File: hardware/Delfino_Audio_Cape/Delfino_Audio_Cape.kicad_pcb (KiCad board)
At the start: 2 copper layers, 143.8 x 162.6 mm, 125 parts, among them J1 JACK_PJ324, J1-J1 Conn_02x10_Odd_Even, J1-J2 Conn_02x10_Odd_Even, J1-J3 Conn_02x10_Odd_Even, J1-J4 Conn_02x10_Odd_Even, J2 JACK_PJ324, J3 JACK_PJ324, J4 PWR, J5 JACK_PJ324, J8 JACK_PJ324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

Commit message: Cambios en el PCB
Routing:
- net +12V: track 729.6 -> 728.8 mm, vias 10 -> 9
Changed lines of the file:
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@@
   (general
     (links 216)
-    (no_connects 0)
+    (no_connects 71)
     (area 111.589943 42.766 277.903715 223.595001)
     (thickness 1.6)
@@
   (segment (start 143.4338 145.2226) (end 143.4338 149.352) (width 0.889) (layer B.Cu) (net 3) (status 20))
   (segment (start 143.4338 149.352) (end 143.3576 149.4282) (width 0.889) (layer B.Cu) (net 3) (status 30))
+  (segment (start 179.8574 138.7348) (end 179.8574 126.9746) (width 2.032) (layer B.Cu) (net 4))
+  (segment (start 179.8574 126.9746) (end 180.213 126.619) (width 2.032) (layer B.Cu) (net 4))
+  (via (at 180.213 126.619) (size 2.54) (drill 0.4) (layers F.Cu B.Cu) (net 4))
+  (segment (start 178.689 82.169) (end 191.389 82.169) (width 2.032) (layer B.Cu) (net 4))
+  (segment (start 197.612 75.946) (end 197.612 64.008) (width 2.032) (layer B.Cu) (net 4))
+  (segment (start 191.389 82.169) (end 197.612 75.946) (width 2.032) (layer B.Cu) (net 4))
+  (segment (start 149.8346 203.0222) (end 119.7356 203.0222) (width 1.27) (layer F.Cu) (net 4))
   (segment (start 171.323 77.851) (end 145.4658 77.851) (width 2.032) (layer B.Cu) (net 4))
   (segment (start 145.4658 77.851) (end 144.8181 78.4987) (width 2.032) (layer B.Cu) (net 4))
@@
   (segment (start 231.394 126.238) (end 180.594 126.238) (width 1.27) (layer F.Cu) (net 4))
   (segment (start 233.1466 124.4854) (end 231.394 126.238) (width 1.27) (layer F.Cu) (net 4))
-  (via (at 178.816 82.296) (size 2.54) (drill 0.4) (layers F.Cu B.Cu) (net 4))
-  (segment (start 197.612 64.008) (end 197.612 77.47) (width 2.032) (layer F.Cu) (net 4))
-  (segment (start 193.04 82.042) (end 197.612 77.47) (width 2.032) (layer F.Cu) (net 4))
-  (segment (start 179.07 82.042) (end 193.04 82.042) (width 2.032) (layer F.Cu) (net 4))
-  (segment (start 179.07 82.042) (end 178.816 82.296) (width 2.032) (layer F.Cu) (net 4))
   (segment (start 233.5276 209.8802) (end 233.5276 207.1116) (width 1.27) (layer F.Cu) (net 4))
   (segment (start 213.36 205.74) (end 179.8574 172.2374) (width 2.032) (layer F.Cu) (net 4))
@@
   (segment (start 180.086 122.555) (end 187.833 114.808) (width 2.032) (layer F.Cu) (net 4))
   (segment (start 180.086 126.619) (end 180.213 126.619) (width 1.27) (layer F.Cu) (net 4))
-  (segment (start 179.8574 138.7348) (end 179.8574 126.9746) (width 2.032) (layer B.Cu) (net 4))
   (segment (start 199.136 147.32) (end 199.136 147.066) (width 1.27) (layer F.Cu) (net 4))
   (segment (start 199.136 147.066) (end 179.324 127.254) (width 2.032) (layer F.Cu) (net 4))
@@
   (segment (start 180.34 126.492) (end 180.34 126.238) (width 2.032) (layer F.Cu) (net 4))
   (segment (start 180.213 126.619) (end 180.34 126.492) (width 2.032) (layer F.Cu) (net 4))
-  (via (at 180.213 126.619) (size 2.54) (drill 0.4) (layers F.Cu B.Cu) (net 4))
-  (segment (start 179.8574 126.9746) (end 180.213 126.619) (width 2.032) (layer B.Cu) (net 4))
   (via (at 188.722 94.742) (size 2.54) (drill 0.4) (layers F.Cu B.Cu) (net 4))
   (segment (start 188.722 94.742) (end 184.404 99.06) (width 2.032) (layer B.Cu) (net 4))
@@
   (segment (start 220.9546 88.0872) (end 220.9546 90.7034) (width 1.27) (layer F.Cu) (net 4))
   (segment (start 171.323 77.851) (end 174.371 77.851) (width 2.032) (layer B.Cu) (net 4))
-  (segment (start 174.371 77.851) (end 178.816 82.296) (width 2.032) (layer B.Cu) (net 4))
+  (segment (start 174.371 77.851) (end 178.689 82.169) (width 2.032) (layer B.Cu) (net 4))
+  (segment (start 178.689 82.169) (end 178.816 82.296) (width 2.032) (layer B.Cu) (net 4))
   (segment (start 178.816 82.296) (end 178.308 81.788) (width 2.032) (layer B.Cu) (net 4))
   (segment (start 178.308 81.788) (end 178.308 99.06) (width 2.032) (layer B.Cu) (net 4))
@@
   (segment (start 119.7356 203.0222) (end 123.2916 199.4662) (width 1.27) (layer B.Cu) (net 4))
   (via (at 119.7356 203.0222) (size 2.54) (drill 0.4) (layers F.Cu B.Cu) (net 4))
-  (segment (start 149.8346 203.0222) (end 119.7356 203.0222) (width 1.27) (layer F.Cu) (net 4))
   (via (at 149.8346 203.0222) (size 2.54) (drill 0.4) (layers F.Cu B.Cu) (net 4))
   (segment (start 149.8346 202.8952) (end 149.8346 203.0222) (width 1.27) (layer B.Cu) (net 4))
@@
   (segment (start 122.1496 178.1662) (end 121.6496 178.6662) (width 0.889) (layer B.Cu) (net 13))
   (segment (start 220.298 154.94) (end 201.1426 154.94) (width 1.27) (layer F.Cu) (net 14))
-  (segment (start 163.5486 117.346) (end 158.464 117.346) (width 1.27) (layer F.Cu) (net 14))
   (segment (start 201.1426 154.94) (end 163.5486 117.346) (width 1.27) (layer F.Cu) (net 14))
+  (segment (start 163.5486 117.346) (end 158.464 117.346) (width 1.27) (layer F.Cu) (net 14))
   (segment (start 141.3256 175.4162) (end 141.2456 175.4162) (width 0.889) (layer B.Cu) (net 15))
   (segment (start 141.2456 175.4162) (end 137.7696 178.8922) (width 0.889) (layer B.Cu) (net 15))
@@
   (segment (start 144.1196 180.4162) (end 141.3256 180.4162) (width 0.889) (layer B.Cu) (net 16))
   (segment (start 144.1196 193.8782) (end 144.1196 198.4502) (width 0.889) (layer B.Cu) (net 17))
+  (segment (start 132.0546 205.3082) (end 132.0546 203.2254) (width 0.889) (layer B.Cu) (net 18))
+  (segment (start 137.7696 197.5104) (end 137.7696 191.3382) (width 0.889) (layer B.Cu) (net 18))
+  (segment (start 132.0546 203.2254) (end 137.7696 197.5104) (width 0.889) (layer B.Cu) (net 18))
   (segment (start 132.0546 210.7692) (end 132.0546 205.3082) (width 0.889) (layer B.Cu) (net 18))
-  (segment (start 137.7696 191.3382) (end 137.7696 199.5932) (width 0.889) (layer B.Cu) (net 18))
-  (segment (start 137.7696 199.5932) (end 132.0546 205.3082) (width 0.889) (layer B.Cu) (net 18))
   (segment (start 128.27 162.052) (end 128.27 154.9038) (width 1.27) (layer B.Cu) (net 19))
   (segment (start 128.27 154.9038) (end 128.4116 154.7622) (width 1.27) (layer B.Cu) (net 19))
@@
     (connect_pads (clearance 0.508))
     (min_thickness 0.254)
-    (fill yes (arc_segments 16) (thermal_gap 0.508) (thermal_bridge_width 0.508))
+    (fill (arc_segments 16) (thermal_gap 0.508) (thermal_bridge_width 0.508))
     (polygon
       (pts
@@
     (connect_pads (clearance 0.508))
     (min_thickness 0.254)
-    (fill yes (arc_segments 16) (thermal_gap 0.508) (thermal_bridge_width 0.508))
+    (fill (arc_segments 16) (thermal_gap 0.508) (thermal_bridge_width 0.508))
     (polygon
       (pts
@@
     (connect_pads (clearance 0.508))
     (min_thickness 0.254)
-    (fill yes (arc_segments 16) (thermal_gap 0.508) (thermal_bridge_width 0.508))
+    (fill (arc_segments 16) (thermal_gap 0.508) (thermal_bridge_width 0.508))
     (polygon
       (pts
@@
     (connect_pads (clearance 0.508))
     (min_thickness 0.254)
-    (fill yes (arc_segments 16) (thermal_gap 0.508) (thermal_bridge_width 0.508))
+    (fill (arc_segments 16) (thermal_gap 0.508) (thermal_bridge_width 0.508))
     (polygon
       (pts
@@
     (connect_pads (clearance 0.508))
     (min_thickness 0.254)
-    (fill yes (arc_segments 16) (thermal_gap 0.508) (thermal_bridge_width 0.508))
+    (fill (arc_segments 16) (thermal_gap 0.508) (thermal_bridge_width 0.508))
     (polygon
       (pts
@@
     (connect_pads (clearance 0.508))
     (min_thickness 0.254)
-    (fill yes (arc_segments 16) (thermal_gap 0.508) (thermal_bridge_width 0.508))
+    (fill (arc_segments 16) (thermal_gap 0.508) (thermal_bridge_width 0.508))
     (polygon
       (pts
@@
     (connect_pads (clearance 0.508))
     (min_thickness 0.254)
-    (fill yes (arc_segments 16) (thermal_gap 0.508) (thermal_bridge_width 0.508))
+    (fill (arc_segments 16) (thermal_gap 0.508) (thermal_bridge_width 0.508))
     (polygon
       (pts
@@
     (connect_pads (clearance 0.508))
     (min_thickness 0.254)
-    (fill yes (arc_segments 16) (thermal_gap 0.508) (thermal_bridge_width 0.508))
+    (fill (arc_segments 16) (thermal_gap 0.508) (thermal_bridge_width 0.508))
     (polygon
       (pts
@@
     (connect_pads (clearance 0.508))
     (min_thickness 0.254)
-    (fill yes (arc_segments 16) (thermal_gap 0.508) (thermal_bridge_width 0.508))
+    (fill (arc_segments 16) (thermal_gap 0.508) (thermal_bridge_width 0.508))
     (polygon
       (pts
@@
     (connect_pads (clearance 0.508))
     (min_thickness 0.254)
-    (fill yes (arc_segments 16) (thermal_gap 0.508) (thermal_bridge_width 0.508))
+    (fill (arc_segments 16) (thermal_gap 0.508) (thermal_bridge_width 0.508))
     (polygon
       (pts
@@
     (connect_pads (clearance 0.508))
     (min_thickness 0.254)
-    (fill yes (arc_segments 16) (thermal_gap 0.508) (thermal_bridge_width 0.508))
+    (fill (arc_segments 16) (thermal_gap 0.508) (thermal_bridge_width 0.508))
     (polygon
       (pts
@@
     (connect_pads (clearance 0.508))
     (min_thickness 0.254)
-    (fill yes (arc_segments 16) (thermal_gap 0.508) (thermal_bridge_width 0.508))
+    (fill (arc_segments 16) (thermal_gap 0.508) (thermal_bridge_width 0.508))
     (polygon
       (pts
@@
     (connect_pads (clearance 0.508))
     (min_thickness 0.254)
-    (fill yes (arc_segments 16) (thermal_gap 0.508) (thermal_bridge_width 0.508))
+    (fill (arc_segments 16) (thermal_gap 0.508) (thermal_bridge_width 0.508))
     (polygon
       (pts
@@
     (connect_pads (clearance 0.508))
     (min_thickness 0.254)
-    (fill yes (arc_segments 16) (thermal_gap 0.508) (thermal_bridge_width 0.508))
+    (fill (arc_segments 16) (thermal_gap 0.508) (thermal_bridge_width 0.508))
     (polygon
       (pts

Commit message: Cambios en el PCB
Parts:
- moved R17 13.7 mm to (153.4, 150.2), turned to 180 degrees
- moved C12 0.20 mm to (148.3, 136.1), turned to 0 degrees
- moved R30 0.20 mm to (123.2, 195.1)
- moved R31 0.20 mm to (127.8, 195.1)
- moved C18 0.20 mm to (149.4, 191.5), turned to 0 degrees
- moved R27 0.13 mm to (144.0, 215.4)
- moved TP15 0.08 mm to (254.1, 190.5)
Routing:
- net +12V: track 728.8 -> 647.3 mm, vias 9 -> 10
- net /ADC_A2: track 65.3 -> 79.1 mm
- net /ADC_A0: track 83.0 -> 76.8 mm, vias 0 -> 2
- net +3V3: track 82.6 -> 88.1 mm, vias 2 -> 4
- net GND: track 5.67 -> 10.4 mm
- net /ADC_B1: track 105.1 -> 107.4 mm, vias 1 -> 2
- added copper zone on B.Cu, net GND
- removed copper zone on F.Cu, net GND
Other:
- net class D1 added: clearance 0.2032, trace_width 0.889, via_dia 2.54, via_drill 0.4
- net class Default: clearance 0.4572 -> 0.508
- rule trace_clearance: 0.4572 -> 0.508

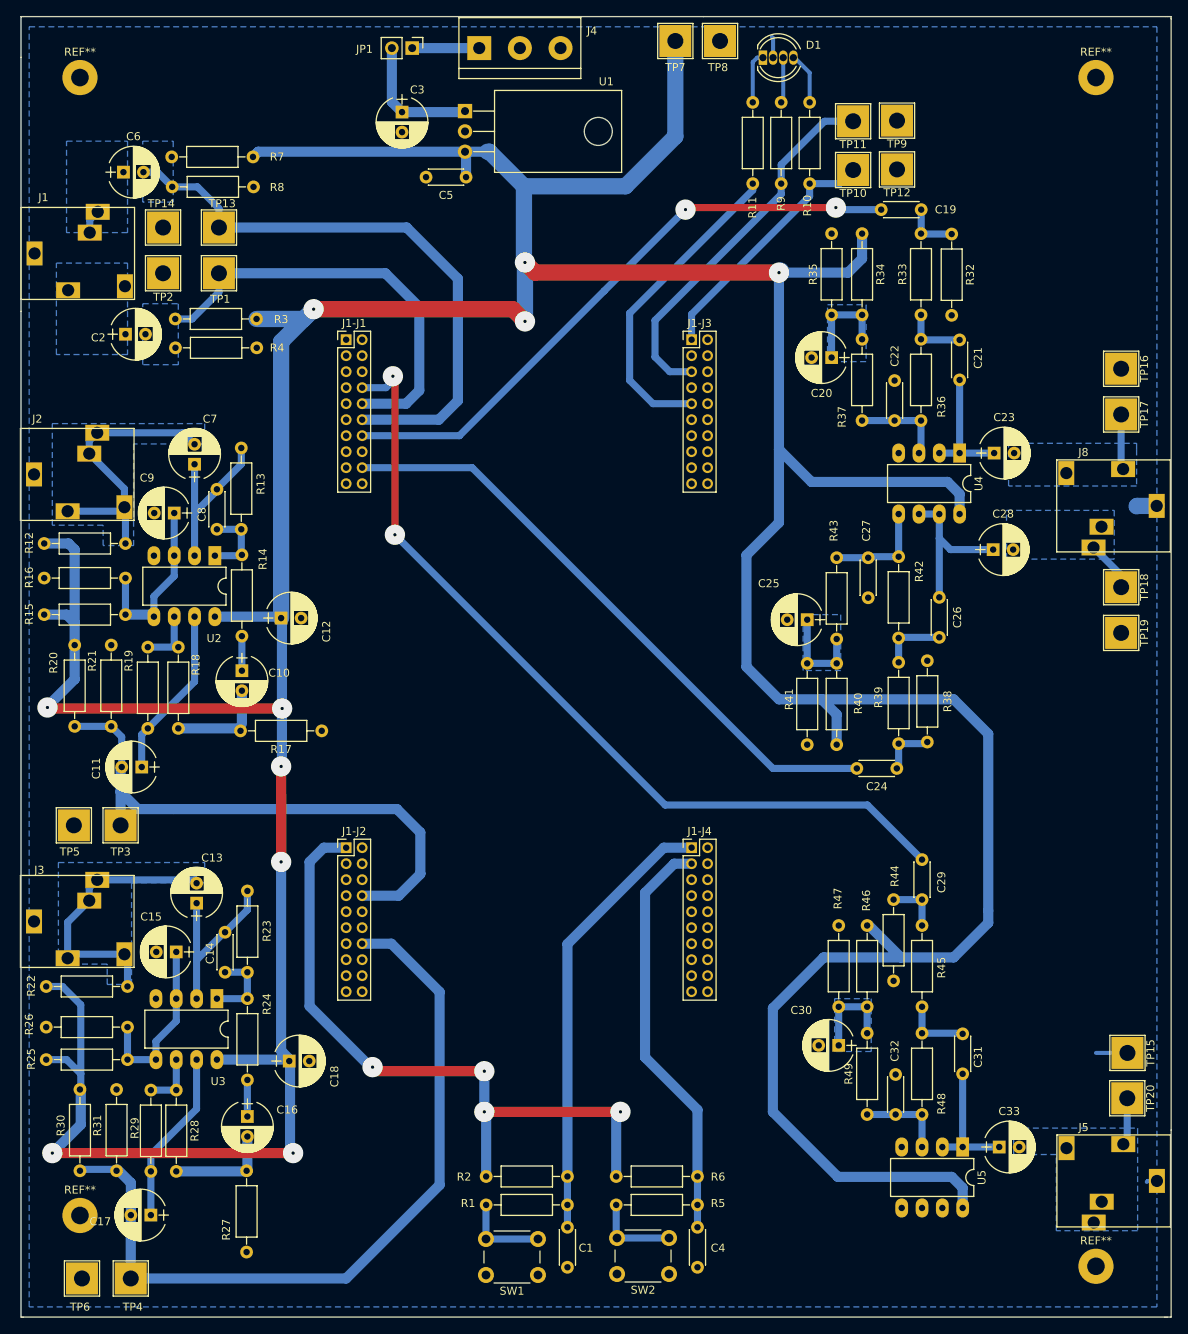
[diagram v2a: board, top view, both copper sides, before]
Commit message: Cambios en el PCB de la tarjeta de expansión
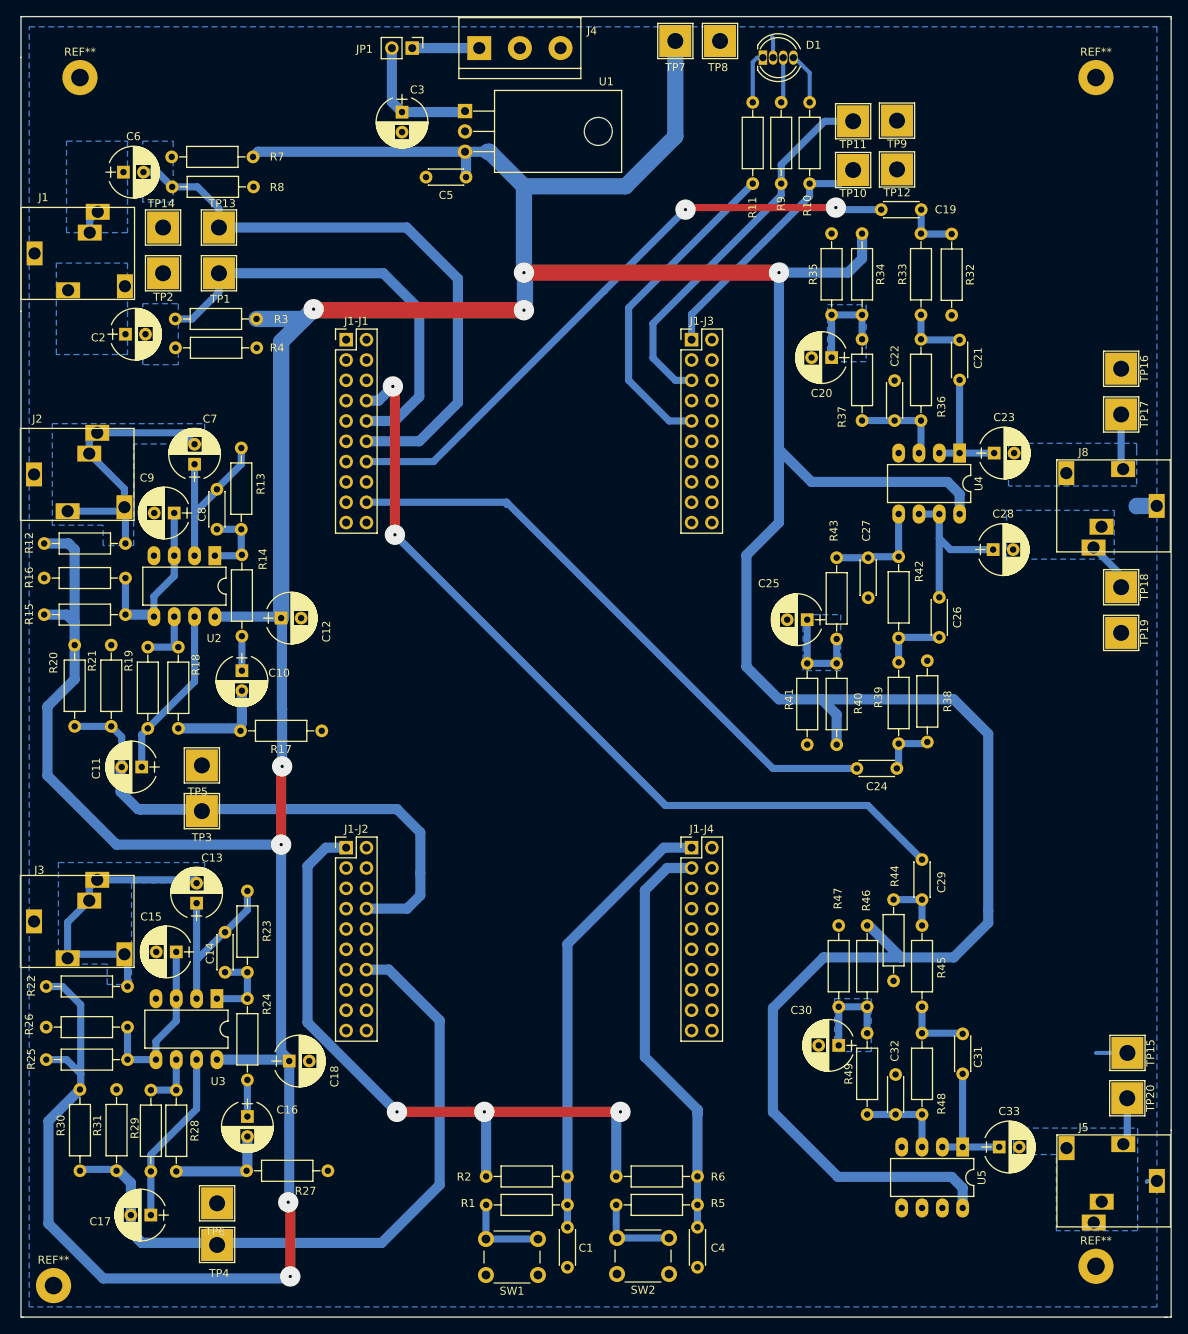
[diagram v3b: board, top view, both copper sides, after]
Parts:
- J1-J1, J1-J2, J1-J3, J1-J4: footprint Pin_Headers:Pin_Header_Straight_2x10_Pitch2.00mm -> Pin_Headers:Pin_Header_Straight_2x10_Pitch2.54mm
- moved TP6 19.3 mm to (140.3, 209.3)
- moved TP5 17.7 mm to (138.4, 154.6)
- moved R27 14.4 mm to (154.2, 205.2), turned to 180 degrees
- moved TP4 11.6 mm to (140.3, 214.5)
- moved TP3 10.3 mm to (138.4, 160.3)
- moved REF** 9.36 mm to (119.9, 219.6)
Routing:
- net /ADC_B1: track 107.4 -> 153.3 mm
- net +12V: track 647.3 -> 676.6 mm, vias 10 -> 8
- net /ADC_A2: track 79.1 -> 82.4 mm
- net +3V3: track 88.1 -> 86.1 mm, vias 4 -> 3
- net /ADC_A1: track 77.4 -> 75.6 mm
- net /PWM_9A: track 39.9 -> 41.0 mm
- net /PWM_8A: track 47.1 -> 48.0 mm
- net /ADC_A0: track 76.8 -> 77.6 mm
- net /ADC_B2: track 74.4 -> 75.1 mm
- net /ADC_B4: track 54.3 -> 54.9 mm

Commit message: Cambios en el PCB
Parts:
- added REF**: VIA-0.6mm, mi_via:VIA-0.6mm, F.Cu at (216.7, 112.3)
- added REF**: VIA-0.6mm, mi_via:VIA-0.6mm, F.Cu at (243.9, 159.1)
- added REF**: VIA-0.6mm, mi_via:VIA-0.6mm, F.Cu at (189.5, 162.9)
- added REF**: VIA-0.6mm, mi_via:VIA-0.6mm, F.Cu at (189.2, 146.0)
- added REF**: VIA-0.6mm, mi_via:VIA-0.6mm, F.Cu at (183.1, 136.9)
- added REF**: VIA-0.6mm, mi_via:VIA-0.6mm, F.Cu at (182.9, 120.5)
- added REF**: VIA-0.6mm, mi_via:VIA-0.6mm, F.Cu at (175.3, 114.6)
- added REF**: VIA-0.6mm, mi_via:VIA-0.6mm, F.Cu at (206.7, 112.8)
- added REF**: VIA-0.6mm, mi_via:VIA-0.6mm, F.Cu at (175.3, 103.6)
- added REF**: VIA-0.6mm, mi_via:VIA-0.6mm, F.Cu at (142.0, 107.7)
- added REF**: VIA-0.6mm, mi_via:VIA-0.6mm, F.Cu at (152.2, 108.0)
- added REF**: VIA-0.6mm, mi_via:VIA-0.6mm, F.Cu at (173.8, 166.2)
- added REF**: VIA-0.6mm, mi_via:VIA-0.6mm, F.Cu at (162.6, 166.2)
- added REF**: VIA-0.6mm, mi_via:VIA-0.6mm, F.Cu at (163.1, 192.4)
- added REF**: VIA-0.6mm, mi_via:VIA-0.6mm, F.Cu at (174.8, 192.4)
- added REF**: VIA-0.6mm, mi_via:VIA-0.6mm, F.Cu at (229.9, 159.1)
- moved TP11 3.18 mm to (220.0, 70.9)
- moved TP9 3.10 mm to (225.3, 70.9)
- moved C6 2.69 mm to (131.3, 80.5), turned to 180 degrees
- moved TP10 2.67 mm to (219.7, 77.5)
- moved TP12 2.59 mm to (225.3, 77.5)
- moved C2 2.44 mm to (131.3, 100.6), turned to 180 degrees
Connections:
- C2 pad 1: /Aux_L -> /ADC_B4
- C2 pad 2: /ADC_B4 -> /Aux_L
- C6 pad 1: /Aux_R -> /ADC_B2
- C6 pad 2: /ADC_B2 -> /Aux_R
- J1-J1 pad 1: (no net) -> Net-(J1-J1-Pad1)
- J1-J1 pad 11: (no net) -> Net-(J1-J1-Pad11)
- J1-J1 pad 13: (no net) -> /SPIA_CLK
- J1-J1 pad 15: (no net) -> /GPIO_61
- J1-J1 pad 16: (no net) -> /ADC_B0
- J1-J1 pad 17: (no net) -> /I2CA_SCL
- J1-J1 pad 19: (no net) -> /I2CA_SDA
- J1-J1 pad 2: (no net) -> Net-(J1-J1-Pad2)
- J1-J1 pad 20: (no net) -> Net-(J1-J1-Pad20)
- J1-J1 pad 3: (no net) -> /GPIO_71
- J1-J1 pad 5: (no net) -> /SCIC_Rx
- J1-J1 pad 6: (no net) -> /ADC_14
- J1-J1 pad 7: (no net) -> /SCIC_Tx
- J1-J1 pad 9: (no net) -> /GPIO_41
- J1-J2 pad 10: (no net) -> /ADC_A5
- J1-J2 pad 11: (no net) -> Net-(J1-J2-Pad11)
- J1-J2 pad 12: (no net) -> /ADC_B5
- J1-J2 pad 13: (no net) -> /SPIB_CLK
- J1-J2 pad 15: (no net) -> Net-(J1-J2-Pad15)
- J1-J2 pad 16: (no net) -> /ADC_B3
- J1-J2 pad 17: (no net) -> /I2CB_SCL
- J1-J2 pad 18: (no net) -> /ADC_A4
- J1-J2 pad 19: (no net) -> /I2CB_SDA
- J1-J2 pad 2: (no net) -> +5V
- J1-J2 pad 20: (no net) -> Net-(J1-J2-Pad20)
- J1-J2 pad 3: (no net) -> Net-(J1-J2-Pad3)
- J1-J2 pad 5: (no net) -> /SCIB_Rx
- J1-J2 pad 6: (no net) -> /ADC_15
- J1-J2 pad 7: (no net) -> /SCIB_Tx
- J1-J2 pad 9: (no net) -> Net-(J1-J2-Pad9)
- J1-J3 pad 10: (no net) -> Net-(J1-J3-Pad10)
- J1-J3 pad 11: (no net) -> /GPIO_17
- J1-J3 pad 12: (no net) -> /SPIA_SIMO
- J1-J3 pad 13: (no net) -> /GPIO_20
- J1-J3 pad 14: (no net) -> /SPIA_SOMI
- J1-J3 pad 15: (no net) -> /GPIO_21
- J1-J3 pad 16: (no net) -> /GPIO_72
- J1-J3 pad 17: (no net) -> /PWM_11A
- J1-J3 pad 18: (no net) -> /GPIO_73
- J1-J3 pad 19: (no net) -> /PWM_11B
- J1-J3 pad 20: (no net) -> /GPIO_78
- J1-J3 pad 3: (no net) -> /GPIO_13
- J1-J3 pad 4: (no net) -> /GPIO_4
- J1-J3 pad 6: (no net) -> /GPIO_62
- J1-J3 pad 7: (no net) -> /GPIO_15
- J1-J3 pad 8: (no net) -> Net-(J1-J3-Pad8)
- J1-J4 pad 10: (no net) -> Net-(J1-J4-Pad10)
- J1-J4 pad 11: (no net) -> /GPIO_19
- J1-J4 pad 12: (no net) -> /GPIO_63
- J1-J4 pad 13: (no net) -> Net-(J1-J4-Pad13)
- J1-J4 pad 14: (no net) -> /GPIO_64
- J1-J4 pad 15: (no net) -> Net-(J1-J4-Pad15)
- J1-J4 pad 16: (no net) -> /GPIO_99
- J1-J4 pad 17: (no net) -> /PWM_10A
- J1-J4 pad 18: (no net) -> /GPIO_92
- J1-J4 pad 19: (no net) -> /PWM_10B
- J1-J4 pad 20: (no net) -> Net-(J1-J4-Pad20)
- J1-J4 pad 4: (no net) -> /GPIO_91
- J1-J4 pad 5: (no net) -> /PWM_6A
- J1-J4 pad 6: (no net) -> Net-(J1-J4-Pad6)
- J1-J4 pad 7: (no net) -> /GPIO_11
- J1-J4 pad 8: (no net) -> Net-(J1-J4-Pad8)
- J1-J4 pad 9: (no net) -> /GPIO_18
- J4 pad 2: (no net) -> Net-(J4-Pad2)
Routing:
- net GND: track 10.4 -> 114.1 mm, vias 0 -> 16
- net +12V: track 676.6 -> 670.1 mm
- net /PWM_7A: track 31.8 -> 33.7 mm
- net /PWM_8A: track 48.0 -> 49.2 mm
- net +3V3: track 86.1 -> 86.0 mm, vias 3 -> 4
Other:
- net class Default: clearance 0.508 -> 0.635
- rule trace_clearance: 0.508 -> 0.635
- board text added: "Launchpad"
